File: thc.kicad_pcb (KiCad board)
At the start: 2 copper layers, 123.8 x 99.7 mm, 75 parts, among them CON1 BARREL_JACK, IC1 4N25, IC2 4N25, IC3 4N25, J2 DB25, J3 DB9, Q1 BC547, U1 LM358, U2 ARDUINO_MINI_PRO, U3 CNY74-4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

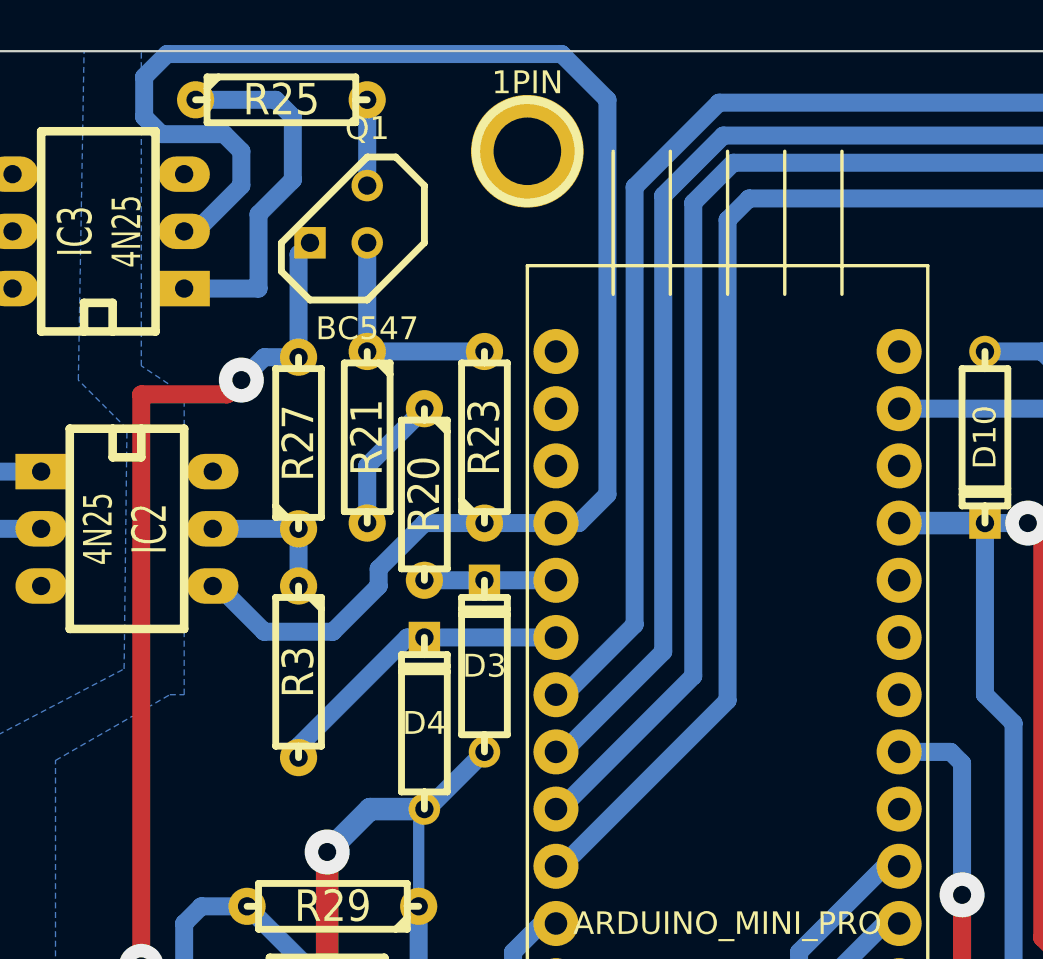
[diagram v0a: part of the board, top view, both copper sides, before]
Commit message: Changed Q1 pulldown to pullup, fixed it's pinout
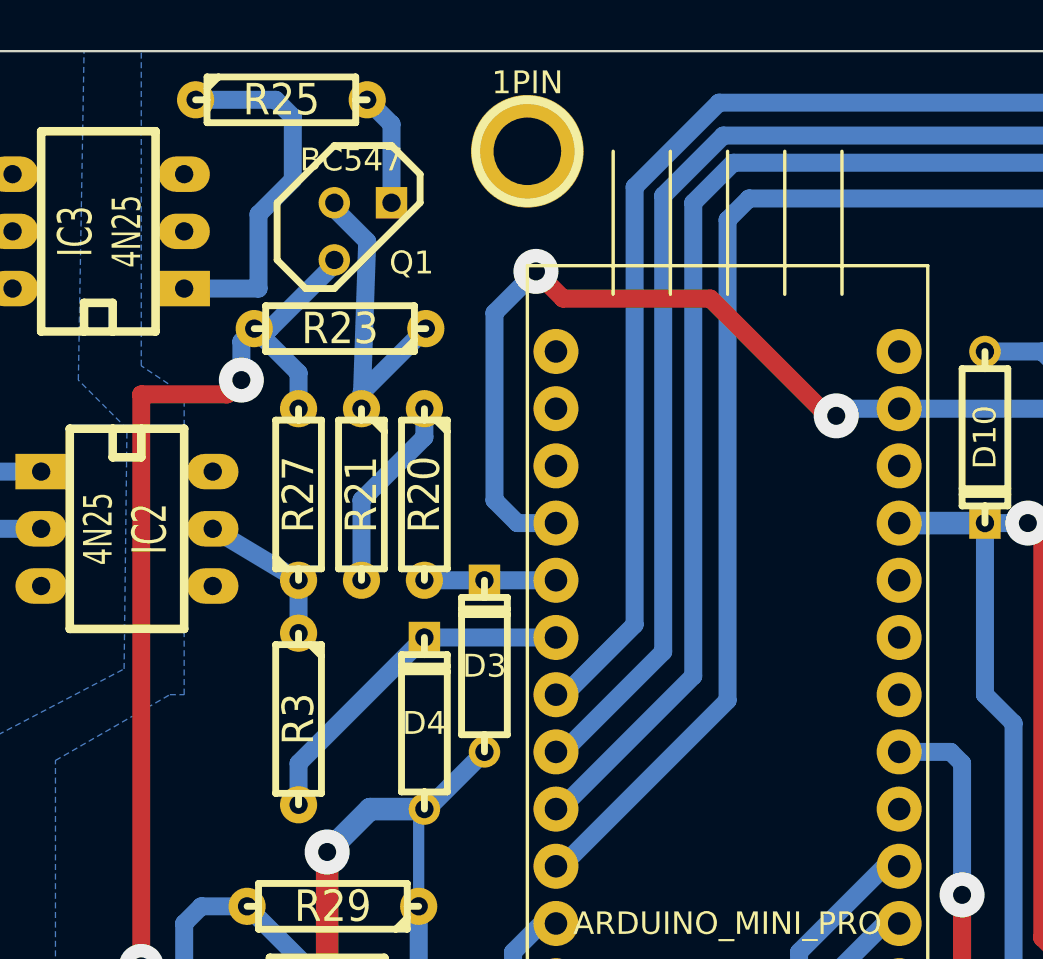
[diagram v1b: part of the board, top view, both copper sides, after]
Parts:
- Q1: footprint TO92 -> TO92-EBC
- R25: value 230R -> 100R
- moved R23 8.03 mm to (71.7, 39.6), turned to 180 degrees
- moved R21 2.55 mm to (72.6, 47.0)
- moved R27 2.29 mm to (69.8, 47.0)
- moved R3 2.10 mm to (69.8, 57.0)
- moved Q1 1.32 mm to (72.7, 35.3), turned to 0 degrees
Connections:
- R23 pad 1: GND -> N-0000072
- R23 pad 2: N-0000072 -> +5V
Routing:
- net GND: track 314.0 -> 274.7 mm, vias 1 -> 3
- net N-0000072: track 10.0 -> 14.5 mm
- net +5V: track 270.4 -> 274.0 mm
- net I_TORCH_ON: track 6.13 -> 8.78 mm
- net N-000002: track 13.9 -> 15.6 mm
- net N-0000074: track 3.81 -> 5.02 mm
